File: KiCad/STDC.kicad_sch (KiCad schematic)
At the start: 17 parts, among them J1 Conn_01x04_Pin, J2 Conn_01x04_Pin, Q1 DMG2302U, U1 STM32L476RGTx, X1 Q13FC1350000400

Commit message: Create Revision 0.0.1
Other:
- company: (none) -> ETH Zurich: Center for Project Based Learning
- title: (none) -> STDC
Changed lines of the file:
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@@
 	(generator_version "9.0")
 	(paper "A4")
+	(title_block
+		(title "STDC")
+		(date "2026-03-05")
+		(rev "0.0.1")
+		(company "ETH Zurich: Center for Project Based Learning")
+	)
 	(rectangle
 		(start 92.075 109.855)

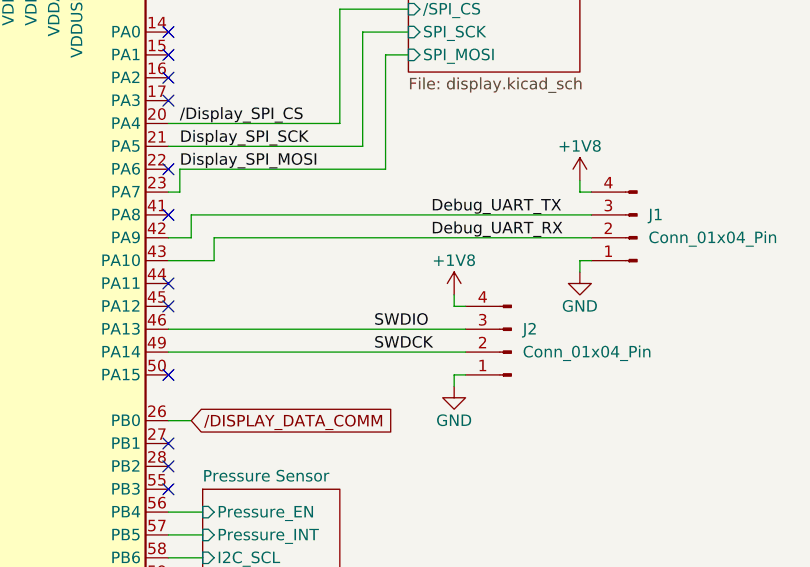
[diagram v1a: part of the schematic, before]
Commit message: Add decoupling for external connectors
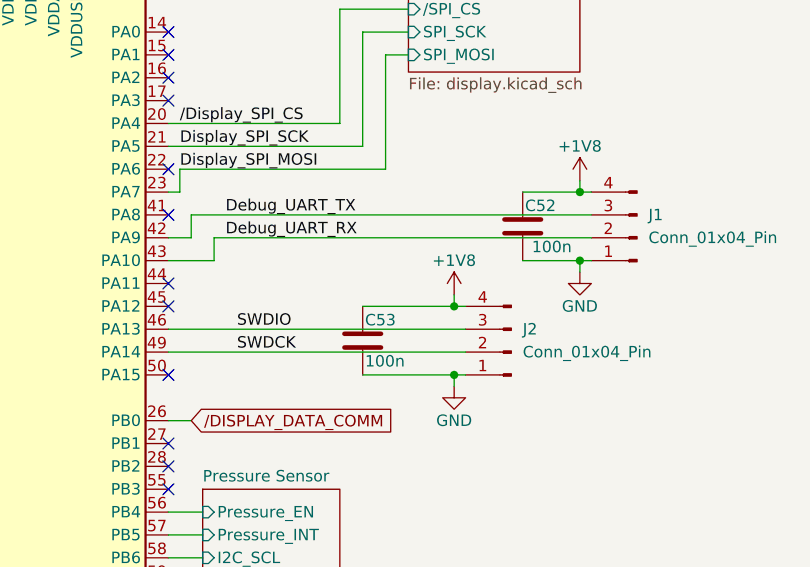
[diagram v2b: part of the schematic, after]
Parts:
- added C52, C53: 100n, Capacitor_SMD:C_0402_1005Metric, symbol Device:C
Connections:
- net +1V8: now also C52.1, C53.1
- net GND: now also C52.2, C53.2
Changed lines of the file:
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@@
 	)
 	(junction
+		(at 198.12 76.2)
+		(diameter 0)
+		(color 0 0 0 0)
+	)
+	(junction
 		(at 82.55 34.29)
 		(diameter 0)
@@
 	)
 	(junction
+		(at 212.09 71.12)
+		(diameter 0)
+		(color 0 0 0 0)
+	)
+	(junction
+		(at 198.12 83.82)
+		(diameter 0)
+		(color 0 0 0 0)
+	)
+	(junction
 		(at 148.59 135.89)
 		(diameter 0)
@@
 	)
 	(junction
+		(at 212.09 63.5)
+		(diameter 0)
+		(color 0 0 0 0)
+	)
+	(junction
 		(at 92.71 34.29)
 		(diameter 0)
@@
 	(wire
 		(pts
+			(xy 187.96 83.82) (xy 198.12 83.82)
+		)
+		(stroke
+			(width 0)
+			(type default)
+		)
+	)
+	(wire
+		(pts
 			(xy 198.12 83.82) (xy 198.12 85.09)
 		)
@@
 	(wire
 		(pts
+			(xy 187.96 76.2) (xy 198.12 76.2)
+		)
+		(stroke
+			(width 0)
+			(type default)
+		)
+	)
+	(wire
+		(pts
 			(xy 92.71 24.13) (xy 102.87 24.13)
 		)
@@
 	(wire
 		(pts
+			(xy 205.74 63.5) (xy 212.09 63.5)
+		)
+		(stroke
+			(width 0)
+			(type default)
+		)
+	)
+	(wire
+		(pts
 			(xy 106.68 80.01) (xy 106.68 78.74)
 		)
@@
 	(wire
 		(pts
+			(xy 205.74 71.12) (xy 212.09 71.12)
+		)
+		(stroke
+			(width 0)
+			(type default)
+		)
+	)
+	(wire
+		(pts
 			(xy 77.47 82.55) (xy 93.98 82.55)
 		)
@@
 	)
 	(label "Debug_UART_RX"
-		(at 195.58 68.58 0)
+		(at 172.72 68.58 0)
 		(effects
 			(font
@@
 	)
 	(label "Debug_UART_TX"
-		(at 195.58 66.04 0)
+		(at 172.72 66.04 0)
 		(effects
 			(font
@@
 	)
 	(label "SWDCK"
-		(at 189.23 81.28 0)
+		(at 173.99 81.28 0)
 		(effects
 			(font
@@
 	)
 	(label "SWDIO"
-		(at 189.23 78.74 0)
+		(at 173.99 78.74 0)
 		(effects
 			(font
@@
 	)
 	(symbol
+		(lib_id "Device:C")
+		(at 205.74 67.31 0)
+		(unit 1)
+		(exclude_from_sim no)
+		(in_bom yes)
+		(on_board yes)
+		(dnp no)
+		(property "Reference" "C52"
+			(at 205.994 65.024 0)
+			(effects
+				(font
+					(size 1.27 1.27)
+				)
+				(justify left)
+			)
+		)
+		(property "Value" "100n"
+			(at 206.756 69.596 0)
+			(effects
+				(font
+					(size 1.27 1.27)
+				)
+				(justify left)
+			)
+		)
+		(property "Footprint" "Capacitor_SMD:C_0402_1005Metric"
+			(at 206.7052 71.12 0)
+			(effects
+				(font
+					(size 1.27 1.27)
+				)
+				(hide yes)
+			)
+		)
+		(property "Datasheet" "~"
+			(at 205.74 67.31 0)
+			(effects
+				(font
+					(size 1.27 1.27)
+				)
+				(hide yes)
+			)
+		)
+		(property "Description" "Unpolarized capacitor"
+			(at 205.74 67.31 0)
+			(effects
+				(font
+					(size 1.27 1.27)
+				)
+				(hide yes)
+			)
+		)
+		(pin "1"
+		)
+		(pin "2"
+		)
+		(instances
+			(project "STDC"
+				(path "/643c756f-a801-466b-9148-7370ee6a5e00"
+					(reference "C52")
+					(unit 1)
+				)
+			)
+		)
+	)
+	(symbol
 		(lib_id "power:GND")
 		(at 72.39 35.56 0)
@@
 					(unit 1)
 				)
+			)
+		)
+	)
+	(symbol
+		(lib_id "Device:C")
+		(at 187.96 80.01 0)
+		(unit 1)
+		(exclude_from_sim no)
+		(in_bom yes)
+		(on_board yes)
+		(dnp no)
+		(property "Reference" "C53"
+			(at 188.214 77.724 0)
+			(effects
+				(font
+					(size 1.27 1.27)
+				)
+				(justify left)
+			)
+		)
+		(property "Value" "100n"
+			(at 188.214 82.296 0)
+			(effects
+				(font
+					(size 1.27 1.27)
+				)
+				(justify left)
+			)
+		)
+		(property "Footprint" "Capacitor_SMD:C_0402_1005Metric"
+			(at 188.9252 83.82 0)
+			(effects
+				(font
+					(size 1.27 1.27)
+				)
+				(hide yes)
+			)
+		)
+		(property "Datasheet" "~"
+			(at 187.96 80.01 0)
+			(effects
+				(font
+					(size 1.27 1.27)
+				)
+				(hide yes)
+			)
+		)
+		(property "Description" "Unpolarized capacitor"
+			(at 187.96 80.01 0)
+			(effects
+				(font
+					(size 1.27 1.27)
+				)
+				(hide yes)
+			)
+		)
+		(pin "1"
+		)
+		(pin "2"
+		)
+		(instances
+			(project "STDC"
+				(path "/643c756f-a801-466b-9148-7370ee6a5e00"
+					(reference "C53")
+					(unit 1)
+				)

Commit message: Added some TODOs, fixed some TODOs
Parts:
- removed C53: 100n, Capacitor_SMD:C_0402_1005Metric, symbol Device:C
- removed J2: Conn_01x04_Pin, Connector:FanPinHeader_1x04_P2.54mm_Vertical, symbol Connector:Conn_01x04_Pin
- added J2: TC2030, Connector:Tag-Connect_TC2030-IDC-NL_2x03_P1.27mm_Vertical, symbol Connector:TC2030
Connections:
- net Pressure Sensor/Pressure_EN: now also U1.61 (PB8); no longer U1.56 (PB4)
- net BLE_TX_IND: now reaches U1.28 (PB2)
- net Flash/SPI_CLK: now reaches U1.34 (PB13)
- net Flash/SPI_MISO: now reaches U1.35 (PB14)
- net Flash/SPI_MOSI: now reaches U1.36 (PB15)
- net /SPI2_CS: now reaches U1.37 (PC6)
- net JTDI: now reaches U1.50 (PA15)
- net JTDO_SWO: now reaches U1.55 (PB3)
- net Bluetooth Module/UART_TX_IND renamed Flash/SPI_NSS
- net Flash_SPI_CLK: no longer names the net of U1.51 (PC10)
- net Flash_SPI_CS: no longer names the net of U1.54 (PD2)
- net Flash_SPI_MISO: no longer names the net of U1.52 (PC11)
- net Flash_SPI_MOSI: no longer names the net of U1.53 (PC12)
- new net JTRST: U1.56 (PB4)
- no-connect marks 27 -> 23
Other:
- sheet Flash ports: added SPI_NSS; removed none
- note added: "TODO: JTAG Pads 10pin J-Link => get KiCad Library?"
- note added: "TODO: More Test LEDs"
- note added: "TODO: Open-Drain"
- note added: "TODO: Pads instead of Connector"
- moved on the sheet: C52

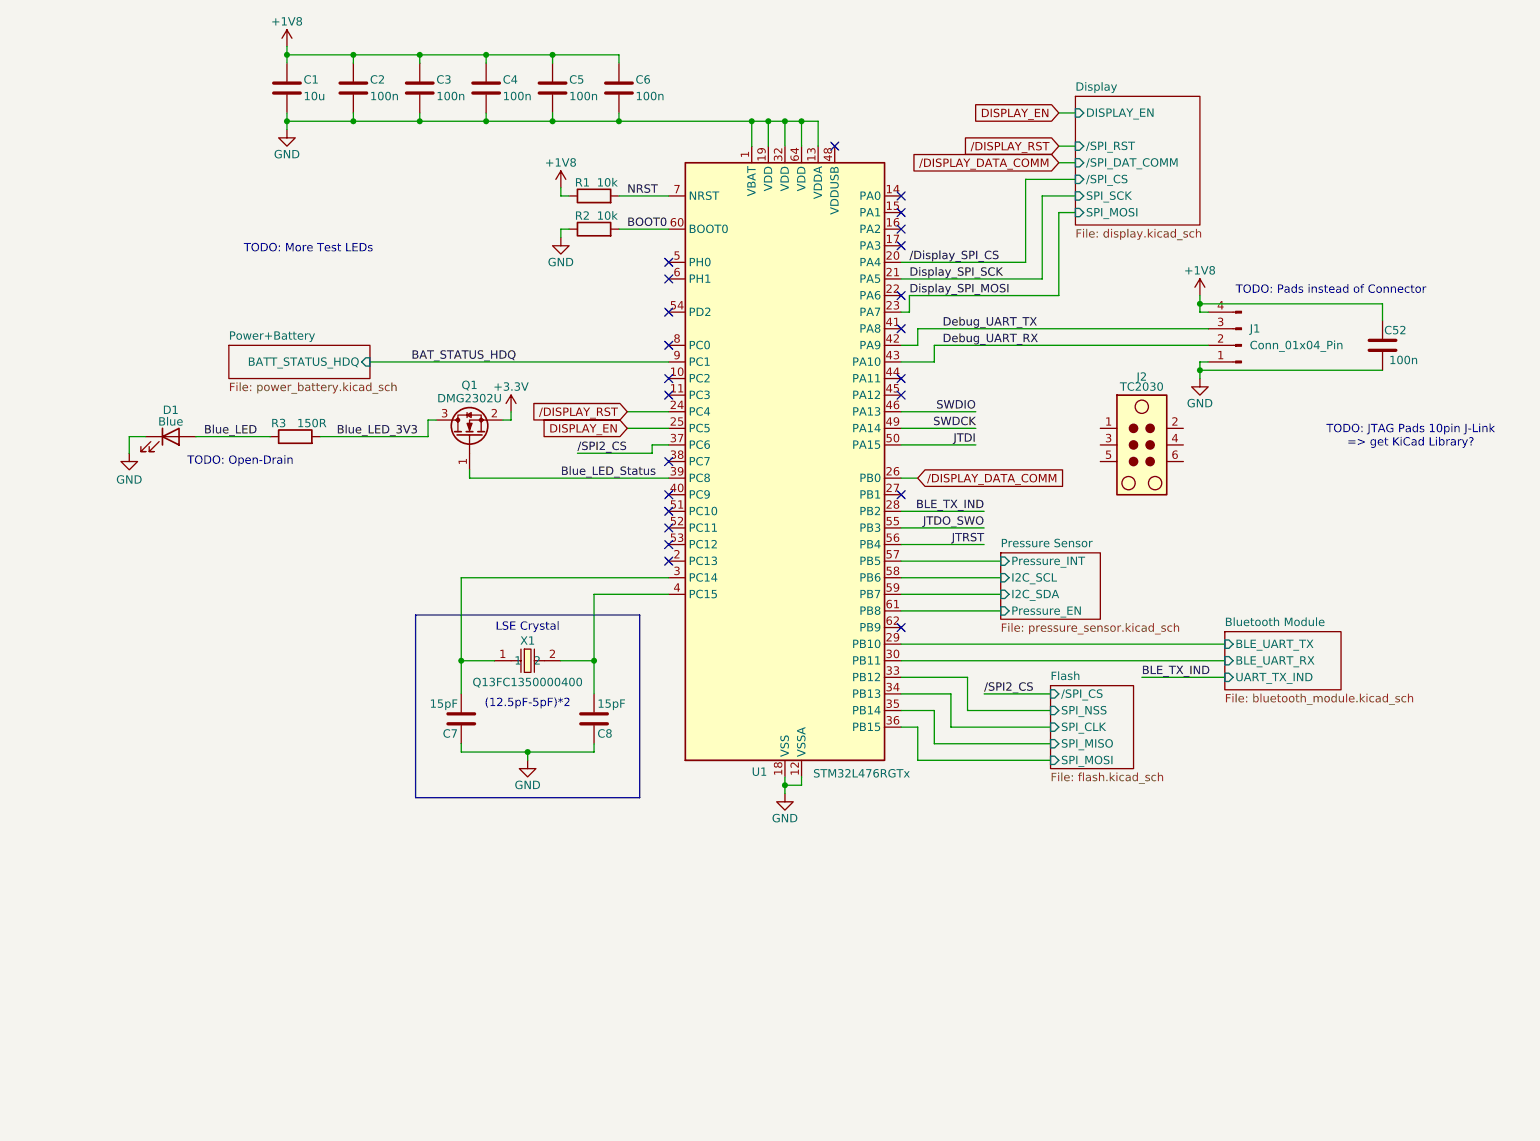
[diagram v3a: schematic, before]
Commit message: Fix JTAG connector
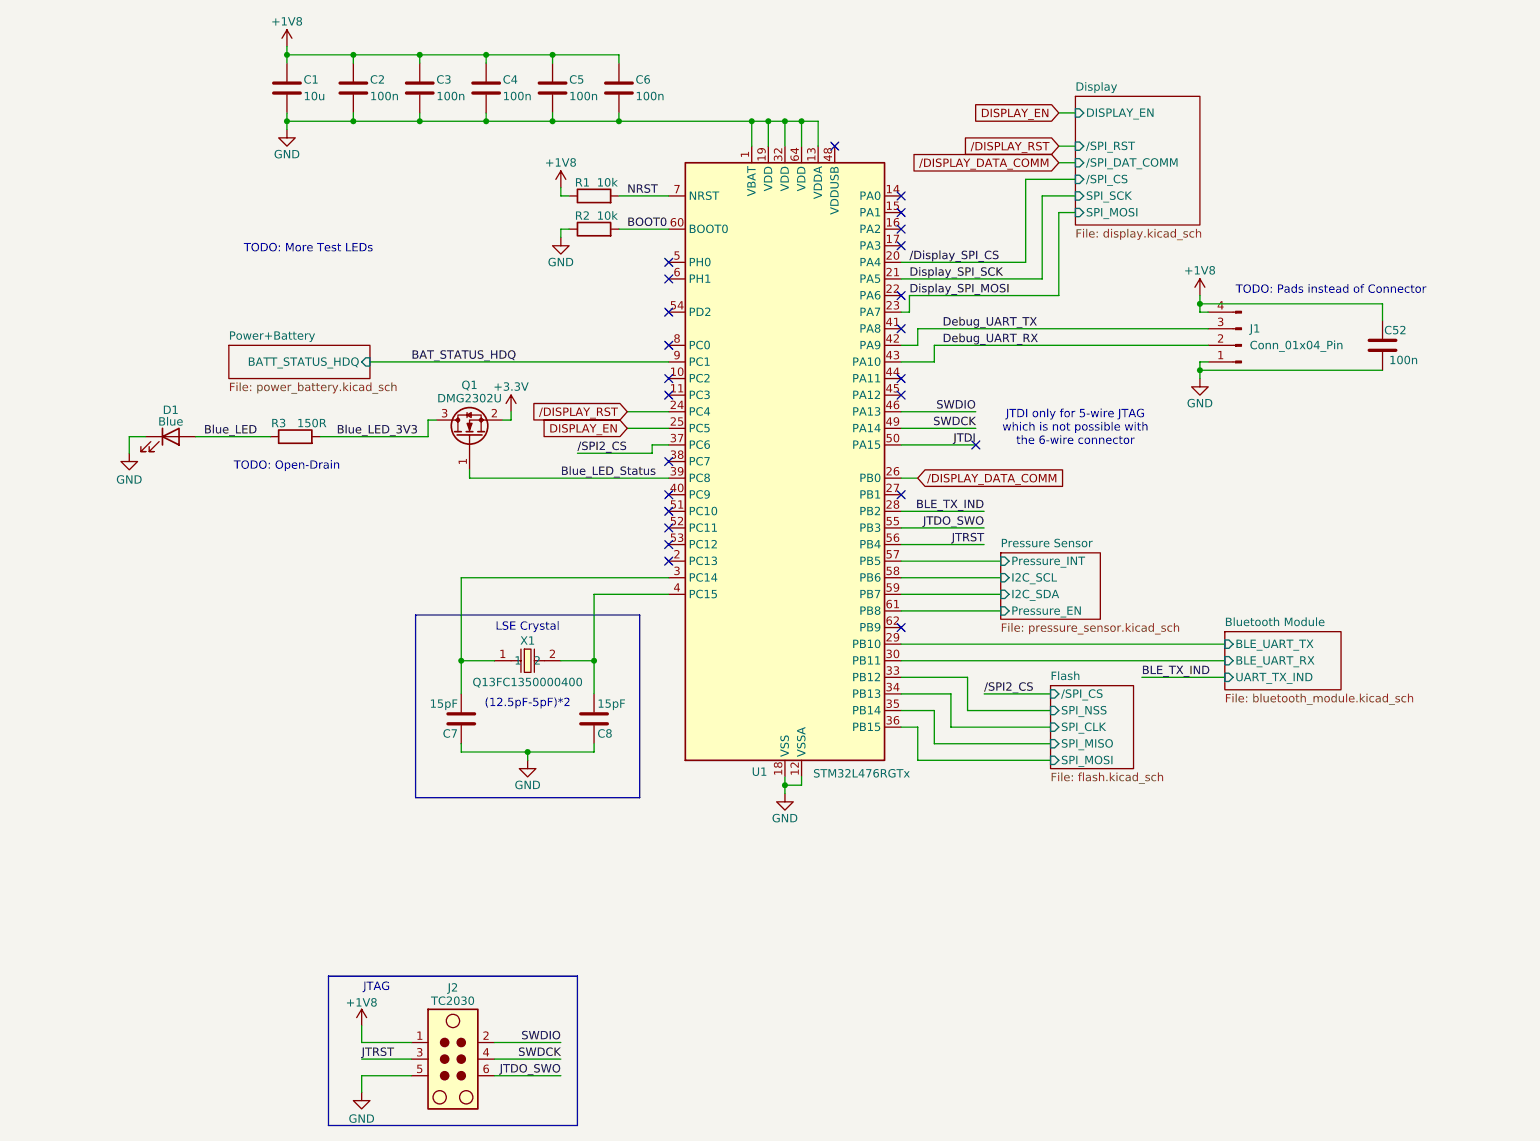
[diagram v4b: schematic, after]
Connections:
- net +1V8: now also J2.1
- net GND: now also J2.5
- net JTDO_SWO: now also J2.6
- net JTRST: now also J2.3
- net SWDCK: now also J2.4
- net SWDIO: now also J2.2
- no-connect marks 23 -> 24
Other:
- note added: "JTAG"
- note added: "JTDI only for 5-wire JTAG which is not possible with the 6-wire connector"
- note removed: "TODO: JTAG Pads 10pin J-Link => get KiCad Library?"
- moved on the sheet: J2

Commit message: Testing connectors, SPI2 pinout, reannotate
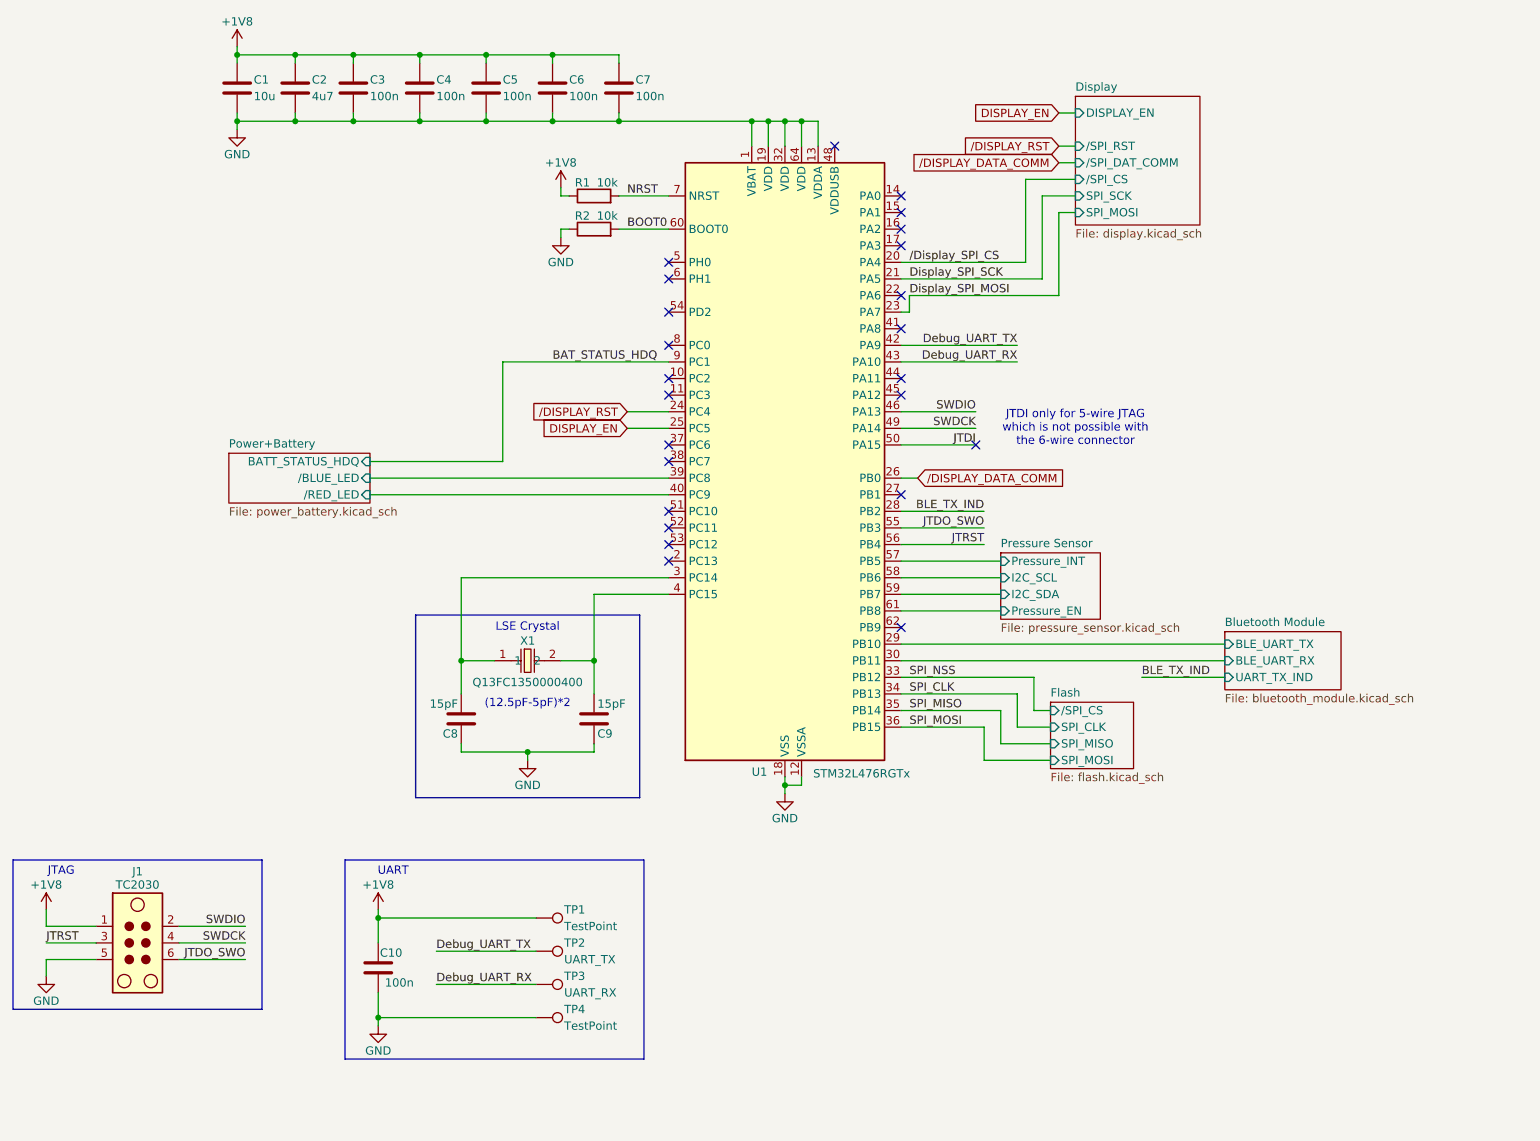
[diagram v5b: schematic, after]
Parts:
- removed C52: 100n, Capacitor_SMD:C_0402_1005Metric, symbol Device:C
- removed D1: Blue, LED_SMD:LED_0603_1608Metric, symbol Device:LED
- removed J1: Conn_01x04_Pin, Connector:FanPinHeader_1x04_P2.54mm_Vertical, symbol Connector:Conn_01x04_Pin
- removed Q1: DMG2302U, Package_TO_SOT_SMD:SOT-23, symbol Transistor_FET:DMG2302U
- removed R3: 150R, Resistor_SMD:R_0402_1005Metric, symbol Device:R
- added C10: 100n, Capacitor_SMD:C_0402_1005Metric, symbol Device:C
- added C2: 4u7, Capacitor_SMD:C_0402_1005Metric, symbol Device:C
- added TP1, TP4: TestPoint, TestPoint:TestPoint_THTPad_2.5x2.5mm_Drill1.2mm, symbol Connector:TestPoint
- added TP2: UART_TX, TestPoint:TestPoint_THTPad_2.5x2.5mm_Drill1.2mm, symbol Connector:TestPoint
- added TP3: UART_RX, TestPoint:TestPoint_THTPad_2.5x2.5mm_Drill1.2mm, symbol Connector:TestPoint
- renumbered C2 to C3, C3 to C4, C4 to C5, C5 to C6, C6 to C7, C7 to C8, C8 to C9, J2 to J1
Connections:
- net +1V8: now also C10.1, C2.1, TP1.1
- net Debug_UART_RX: now also TP3.1
- net Debug_UART_TX: now also TP2.1
- net GND: now also C10.2, C2.2, TP4.1
- net Power+Battery//RED_LED: now reaches U1.40 (PC9)
- net Blue_LED_Status renamed Power+Battery//BLUE_LED
- net Flash/SPI_CLK renamed SPI_CLK
- net Flash/SPI_MISO renamed SPI_MISO
- net Flash/SPI_MOSI renamed SPI_MOSI
- net Flash/SPI_NSS renamed SPI_NSS
- net /SPI2_CS: no longer names the net of U1.37 (PC6)
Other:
- sheet Flash ports: added none; removed SPI_NSS
- sheet Power+Battery ports: added /BLUE_LED, /RED_LED; removed none
- note added: "UART"
- note removed: "TODO: More Test LEDs"
- note removed: "TODO: Open-Drain"
- note removed: "TODO: Pads instead of Connector"
- moved on the sheet: C1, J1

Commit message: Fix display Rs to fix 17V reference and consolidate BOM
And add more info to R_{IREF}
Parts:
- TP1, TP2, TP3, TP4: now left out of the parts list
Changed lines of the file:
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@@
 		(unit 1)
 		(exclude_from_sim no)
-		(in_bom yes)
+		(in_bom no)
 		(on_board yes)
 		(dnp no)
@@
 		(unit 1)
 		(exclude_from_sim no)
-		(in_bom yes)
+		(in_bom no)
 		(on_board yes)
 		(dnp no)
@@
 		(unit 1)
 		(exclude_from_sim no)
-		(in_bom yes)
+		(in_bom no)
 		(on_board yes)
 		(dnp no)
@@
 		(unit 1)
 		(exclude_from_sim no)
-		(in_bom yes)
-		(on_board yes)
-		(dnp no)
+		(in_bom no)
+		(on_board yes)
+		(dnp no)

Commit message: First Draft PCB Layout
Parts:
- added C4: 10n, Capacitor_SMD:C_0402_1005Metric, symbol Device:C
- C1: value 10u -> 4u7
- C3: value 100n -> 1u
- TP1, TP2, TP3, TP4: footprint TestPoint:TestPoint_THTPad_2.5x2.5mm_Drill1.2mm -> TestPoint:TestPoint_THTPad_1.0x1.0mm_Drill0.5mm
- renumbered C9 to C10, C10 to C11, C4 to C5, C5 to C6, C6 to C7, C7 to C8, C8 to C9
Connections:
- net +1V8: now also U1.1 (VBAT), U1.13 (VDDA), U1.19 (VDD), U1.32 (VDD), U1.64 (VDD), C4.1
- net GND: now also C4.2; no longer U1.1 (VBAT), U1.13 (VDDA), U1.19 (VDD), U1.32 (VDD), U1.64 (VDD)
- net LSE_14: now reaches C9.2, U1.3 (PC14), X1.1
- net LSE_15: now reaches C10.2, U1.4 (PC15), X1.2
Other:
- moved on the sheet: C1, C2, C3, C5, C6, C7, C8
